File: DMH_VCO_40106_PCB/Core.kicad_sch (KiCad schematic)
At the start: 66 parts, among them Q1 BC558, Q2 BC548, U1 40106, U2 TL074, U3 TL074, U4 TL074

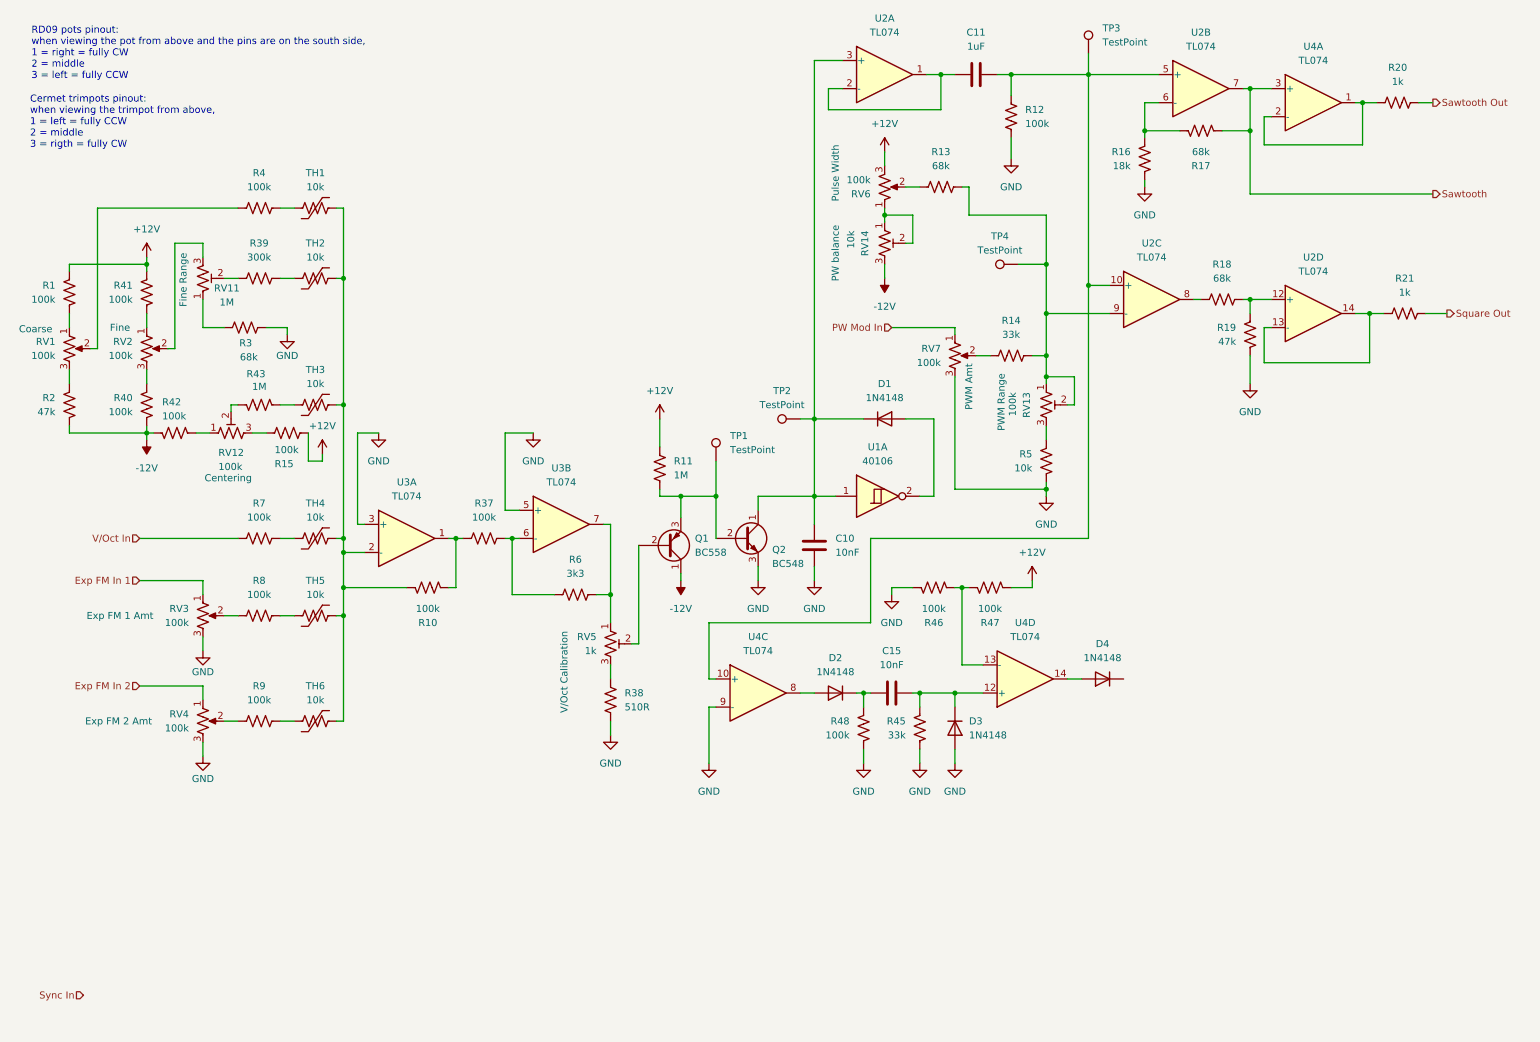
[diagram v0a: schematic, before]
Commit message: Finished Sync input design
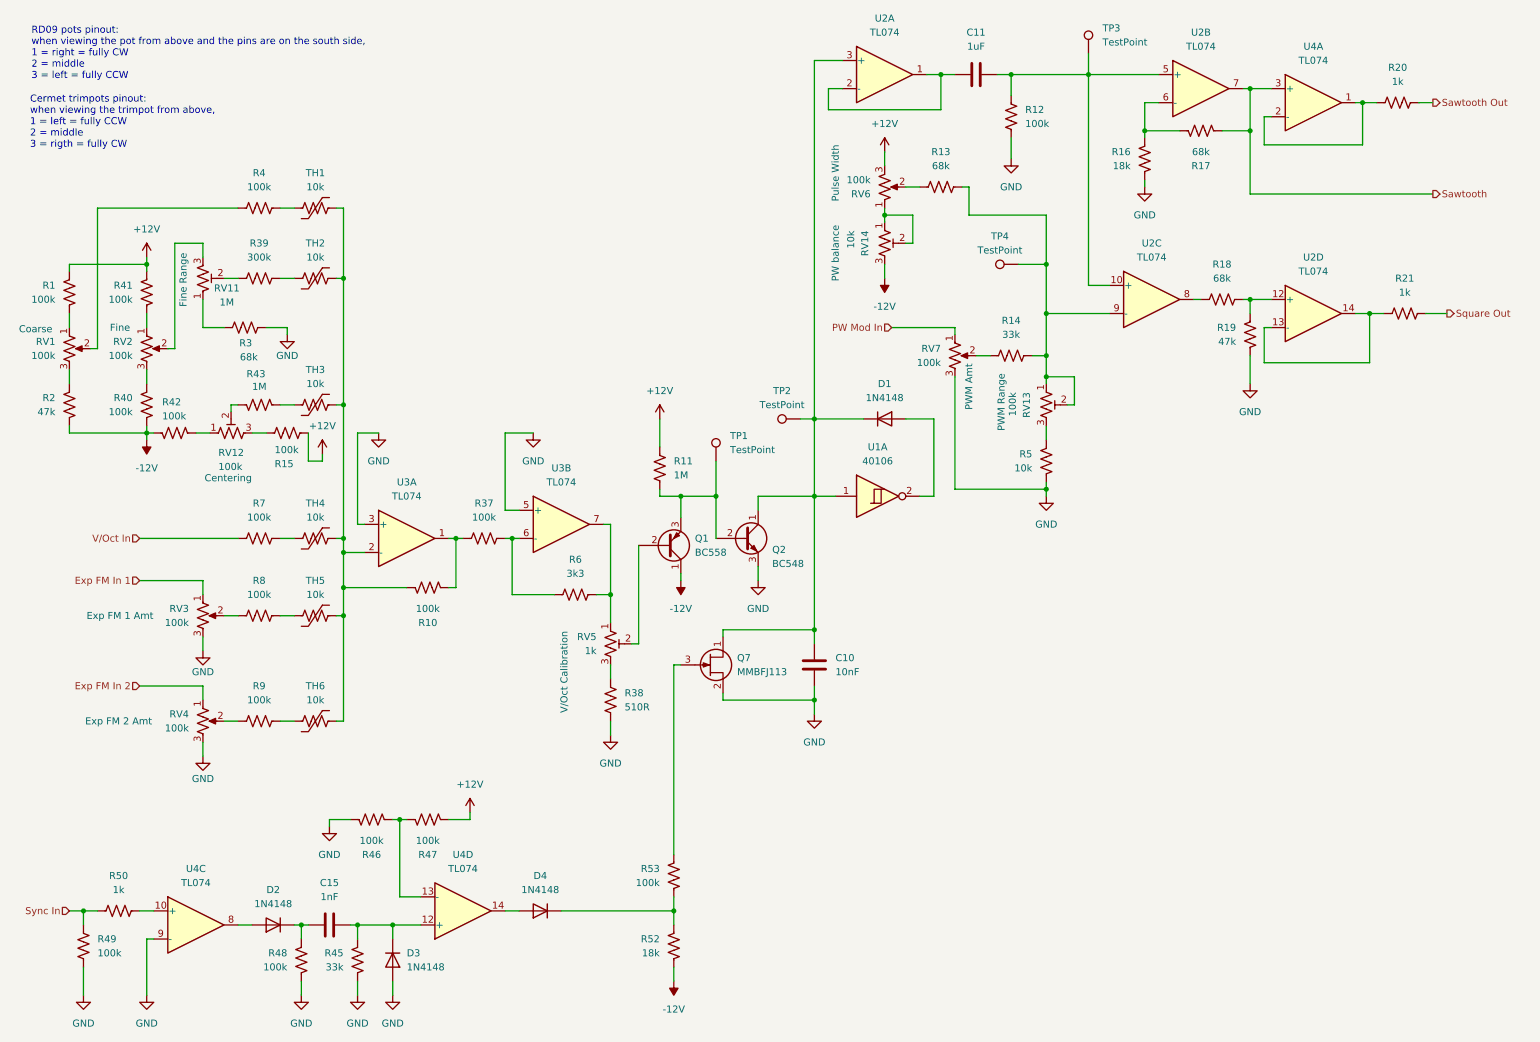
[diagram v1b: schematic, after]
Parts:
- added Q7: MMBFJ113, Package_TO_SOT_SMD:SOT-23, symbol Transistor_FET:MMBFJ113
- added R49, R53: 100k, Resistor_THT:R_Axial_DIN0204_L3.6mm_D1.6mm_P5.08mm_Horizontal, symbol Device:R_US
- added R50: 1k, Resistor_THT:R_Axial_DIN0204_L3.6mm_D1.6mm_P5.08mm_Horizontal, symbol Device:R_US
- added R52: 18k, Resistor_THT:R_Axial_DIN0204_L3.6mm_D1.6mm_P5.08mm_Horizontal, symbol Device:R_US
- C15: value 10nF -> 1nF
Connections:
- net -12V: now also R52.2
- net GND: now also Q7.2 (S), R49.1
- net Sync In: now also R49.2, R50.2
- net at C11.2, R12.2, TP3.1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: no longer U4.10 (+)
- net at C10.1, D1.1 (K), Q2.1 (C)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: now also Q7.1 (D)
- net at D4.1 (K): now also R52.1, R53.2
- new net: Q7.3 (G), R53.1
- new net: R50.1, U4.10 (+)
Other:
- moved on the sheet: C10, C15, D2, D3, D4, R45, R46, R47, R48, U4C, U4D

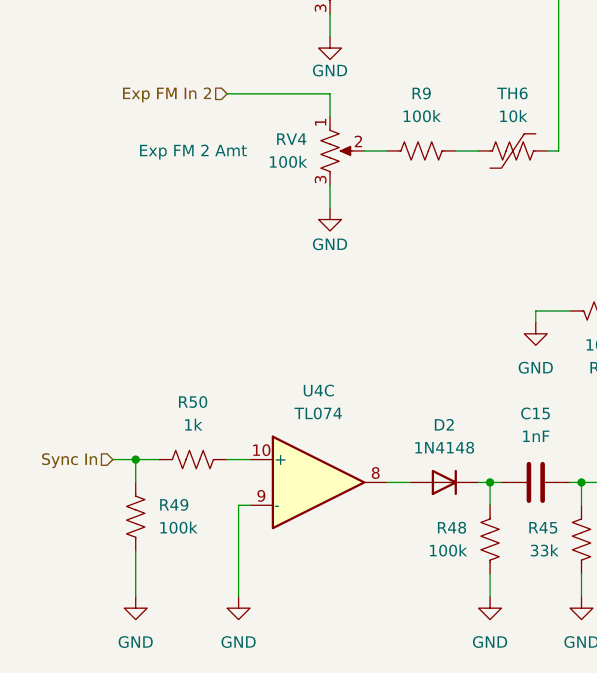
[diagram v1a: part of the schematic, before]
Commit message: Fixed bug on sync input circuit
... in order to keep the pulse generator quiet when no signal is connected to the sync input.
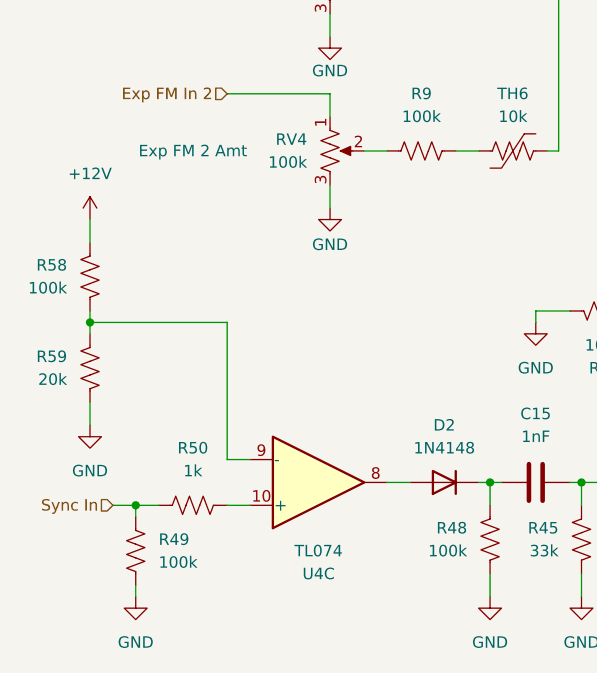
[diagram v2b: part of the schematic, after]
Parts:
- added R58: 100k, Resistor_THT:R_Axial_DIN0204_L3.6mm_D1.6mm_P5.08mm_Horizontal, symbol Device:R_US
- added R59: 20k, Resistor_THT:R_Axial_DIN0204_L3.6mm_D1.6mm_P5.08mm_Horizontal, symbol Device:R_US
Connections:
- net +12V: now also R58.1
- net GND: now also R59.2; no longer U4.9 (-)
- new net: R58.2, R59.1, U4.9 (-)
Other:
- moved on the sheet: R49, R50

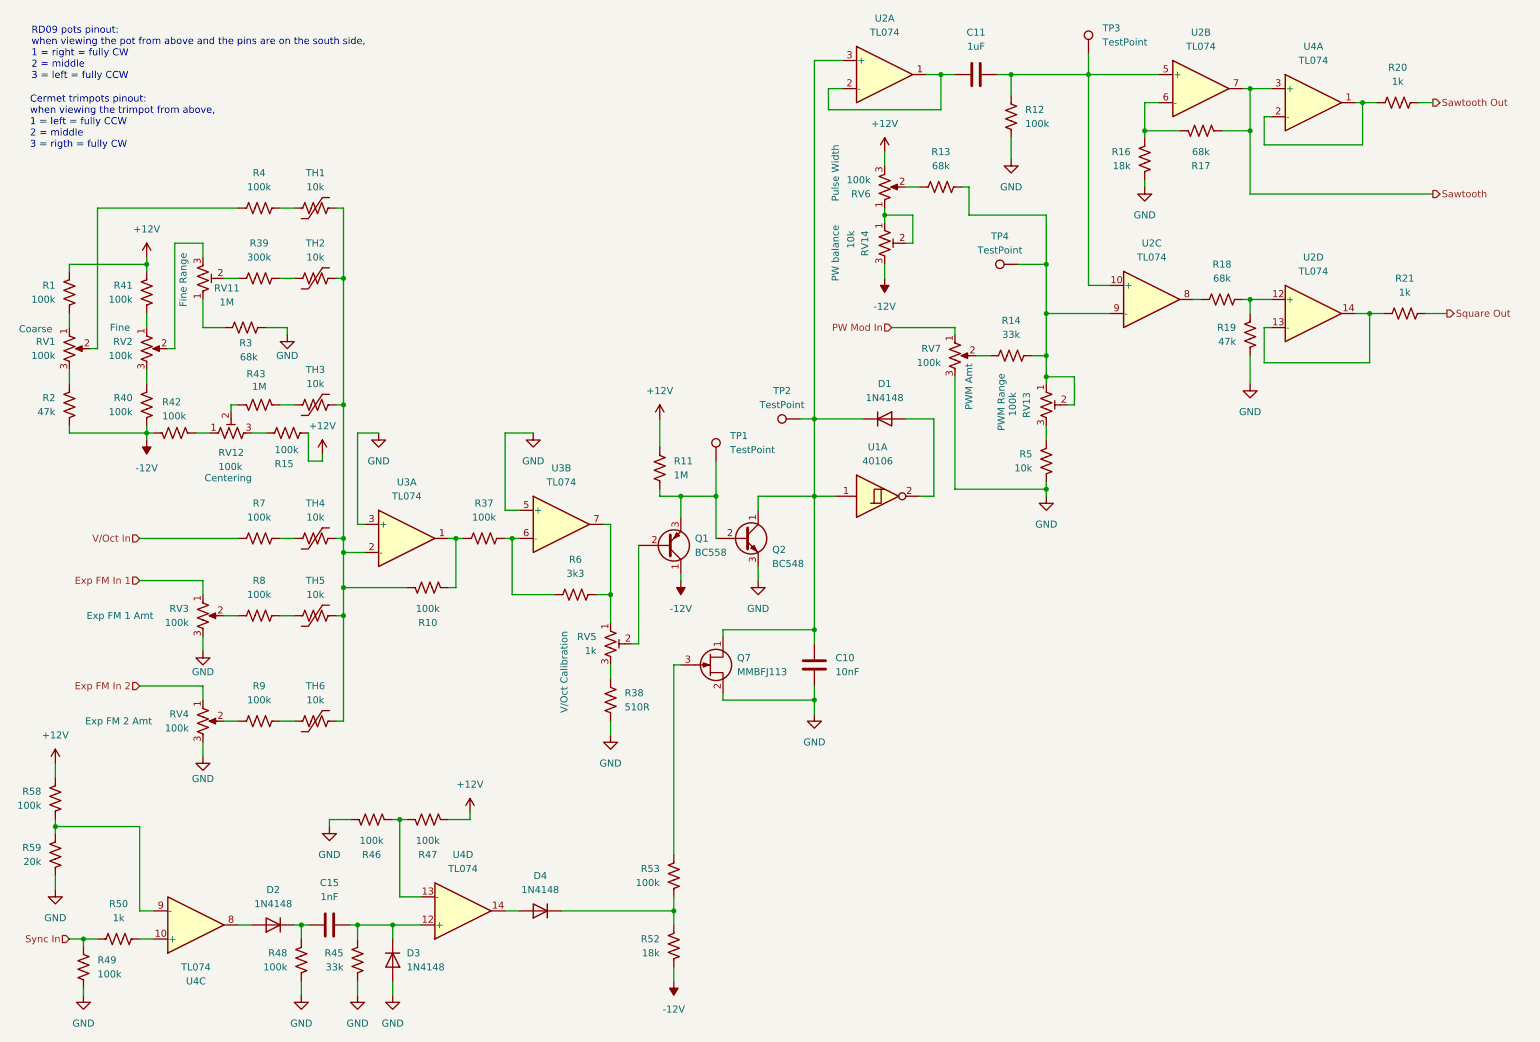
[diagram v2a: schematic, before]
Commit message: Updated Tuner
- Changed uC to ATtiny4313
- Added LEDs
- Created "function" field and updated all jacks, switches and pots
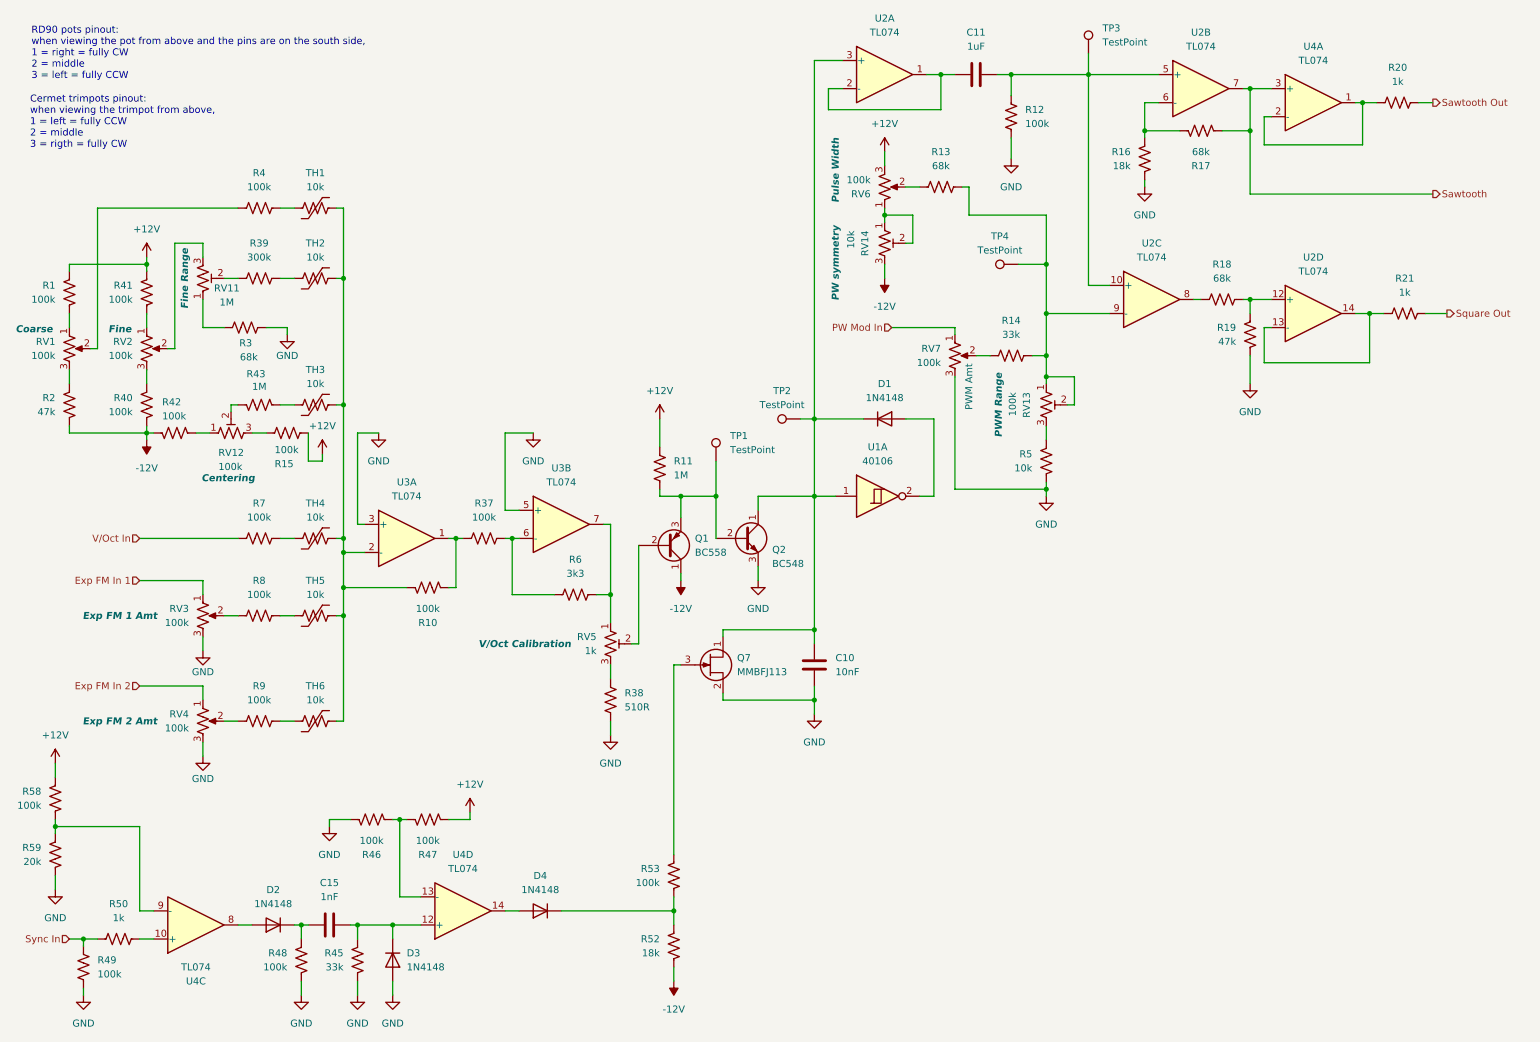
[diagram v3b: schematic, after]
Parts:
- RV1: Function (none) -> Coarse
- RV11: Function (none) -> Fine Range
- RV14: Function PW balance -> PW symmetry
- RV2: Function (none) -> Fine
- RV3: Function (none) -> Exp FM 1 Amt
- RV4: Function (none) -> Exp FM 2 Amt
- RV5: Function (none) -> V/Oct Calibration
- RV6: Function (none) -> Pulse Width
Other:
- note added: "RD90 pots pinout: when viewing the pot from above and the pins are on the south side, 1 = right = fully CW 2 = middle 3 = left = fully CCW"
- note removed: "RD09 pots pinout: when viewing the pot from above and the pins are on the south side, 1 = right = fully CW 2 = middle 3 = left = fully CCW"
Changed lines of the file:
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@@
 		)
 	)
-	(text "RD09 pots pinout:\nwhen viewing the pot from above and the pins are on the south side,\n1 = right = fully CW\n2 = middle\n3 = left = fully CCW"
+	(text "RD90 pots pinout:\nwhen viewing the pot from above and the pins are on the south side,\n1 = right = fully CW\n2 = middle\n3 = left = fully CCW"
 		(exclude_from_sim no)
 		(at 16.002 20.32 0)
@@
 			)
 		)
-		(property "Description" "Fine Range"
+		(property "Description" ""
 			(at 43.434 61.214 90)
 			(effects
@@
 					(size 1.27 1.27)
 				)
+				(hide yes)
+			)
+		)
+		(property "Function" "Fine Range"
+			(at 43.688 60.96 90)
+			(effects
+				(font
+					(size 1.27 1.27)
+					(bold yes)
+					(italic yes)
+				)
 			)
 		)
@@
 			)
 		)
-		(property "Function" "PW balance"
-			(at 161.29 56.388 90)
+		(property "Function" "PW symmetry"
+			(at 161.29 58.166 90)
 			(effects
 				(font
 					(size 1.27 1.27)
+					(bold yes)
+					(italic yes)
 				)
 			)
@@
 			)
 		)
-		(property "Description" "Exp FM 1 Amt"
+		(property "Description" ""
+			(at 32.004 121.92 0)
+			(effects
+				(font
+					(size 1.27 1.27)
+				)
+				(hide yes)
+			)
+		)
+		(property "Function" "Exp FM 1 Amt"
 			(at 32.004 121.92 0)
 			(effects
 				(font
 					(size 1.27 1.27)
+					(bold yes)
+					(italic yes)
 				)
 			)
@@
 			)
 		)
-		(property "Description" "Pulse Width"
+		(property "Description" ""
 			(at 161.29 41.91 90)
 			(effects
@@
 					(size 1.27 1.27)
 				)
+				(hide yes)
+			)
+		)
+		(property "Function" "Pulse Width"
+			(at 161.29 41.402 90)
+			(effects
+				(font
+					(size 1.27 1.27)
+					(bold yes)
+					(italic yes)
+				)
 			)
 		)
@@
 			)
 		)
-		(property "Description" "V/Oct Calibration"
+		(property "Description" ""
 			(at 112.268 132.08 90)
 			(effects
@@
 					(size 1.27 1.27)
 				)
+				(hide yes)
+			)
+		)
+		(property "Function" "V/Oct Calibration"
+			(at 105.156 127 0)
+			(effects
+				(font
+					(size 1.27 1.27)
+					(bold yes)
+					(italic yes)
+				)
 			)
 		)
@@
 		)
 		(property "Function" "PWM Range"
-			(at 191.262 83.312 90)
+			(at 190.754 83.82 90)
 			(effects
 				(font
 					(size 1.27 1.27)
+					(bold yes)
+					(italic yes)
 				)
 			)
@@
 			)
 		)
-		(property "Description" "Fine"
+		(property "Description" ""
 			(at 32.004 69.85 0)
 			(effects
@@
 					(size 1.27 1.27)
 				)
+				(hide yes)
+			)
+		)
+		(property "Function" "Fine"
+			(at 32.004 70.104 0)
+			(effects
+				(font
+					(size 1.27 1.27)
+					(bold yes)
+					(italic yes)
+				)
 			)
 		)
@@
 				(font
 					(size 1.27 1.27)
+					(bold yes)
+					(italic yes)
 				)
 			)
@@
 			)
 		)
-		(property "Description" "Coarse"
+		(property "Description" ""
 			(at 16.764 70.104 0)
 			(effects
@@
 					(size 1.27 1.27)
 				)
+				(hide yes)
+			)
+		)
+		(property "Function" "Coarse"
+			(at 16.51 70.104 0)
+			(effects
+				(font
+					(size 1.27 1.27)
+					(bold yes)
+					(italic yes)
+				)
 			)
 		)
@@
 			)
 		)
-		(property "Description" "Exp FM 2 Amt"
+		(property "Description" ""
 			(at 31.75 140.97 0)
 			(effects
@@
 					(size 1.27 1.27)
 				)
+				(hide yes)
+			)
+		)
+		(property "Function" "Exp FM 2 Amt"
+			(at 32.004 140.97 0)
+			(effects
+				(font
+					(size 1.27 1.27)
+					(bold yes)
+					(italic yes)
+				)
 			)

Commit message: Fixed trimpot fp linking
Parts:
- RV11, RV12, RV13, RV14: footprint Resistor_THT:R_Axial_DIN0204_L3.6mm_D1.6mm_P5.08mm_Horizontal -> Potentiometer_THT:Potentiometer_Bourns_3296W_Vertical
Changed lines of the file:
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@@
 			)
 		)
-		(property "Footprint" "Resistor_THT:R_Axial_DIN0204_L3.6mm_D1.6mm_P5.08mm_Horizontal"
+		(property "Footprint" "Potentiometer_THT:Potentiometer_Bourns_3296W_Vertical"
 			(at 46.99 60.96 0)
 			(effects
@@
 			)
 		)
-		(property "Footprint" "Resistor_THT:R_Axial_DIN0204_L3.6mm_D1.6mm_P5.08mm_Horizontal"
+		(property "Footprint" "Potentiometer_THT:Potentiometer_Bourns_3296W_Vertical"
 			(at 170.18 54.61 0)
 			(effects
@@
 			)
 		)
-		(property "Footprint" "Resistor_THT:R_Axial_DIN0204_L3.6mm_D1.6mm_P5.08mm_Horizontal"
+		(property "Footprint" "Potentiometer_THT:Potentiometer_Bourns_3296W_Vertical"
 			(at 199.39 83.82 0)
 			(effects
@@
 			)
 		)
-		(property "Footprint" "Resistor_THT:R_Axial_DIN0204_L3.6mm_D1.6mm_P5.08mm_Horizontal"
+		(property "Footprint" "Potentiometer_THT:Potentiometer_Bourns_3296W_Vertical"
 			(at 52.07 88.9 0)
 			(effects
